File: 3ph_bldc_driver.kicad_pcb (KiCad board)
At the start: 4 copper layers, 20 parts, among them Q1 AON7264E-HXY, Q2 AON7264E-HXY, Q3 AON7264E-HXY, Q4 AON7264E-HXY, Q5 AON7264E-HXY, Q6 AON7264E-HXY

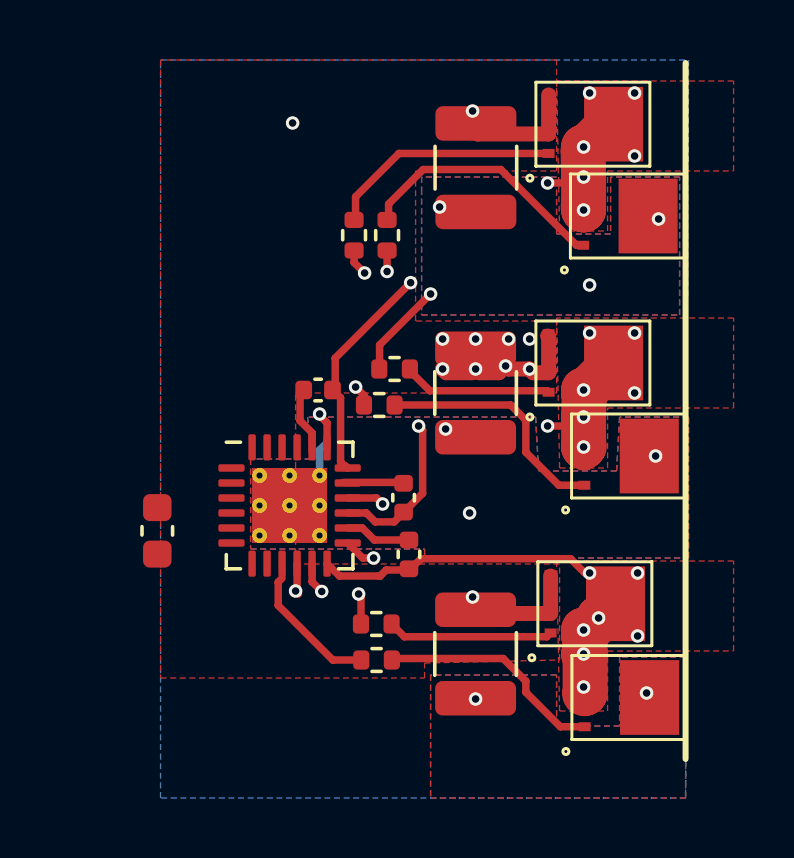
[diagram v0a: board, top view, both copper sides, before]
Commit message: found real parts for capacitors, added 0 ohm resistors, added diode footprints for src line
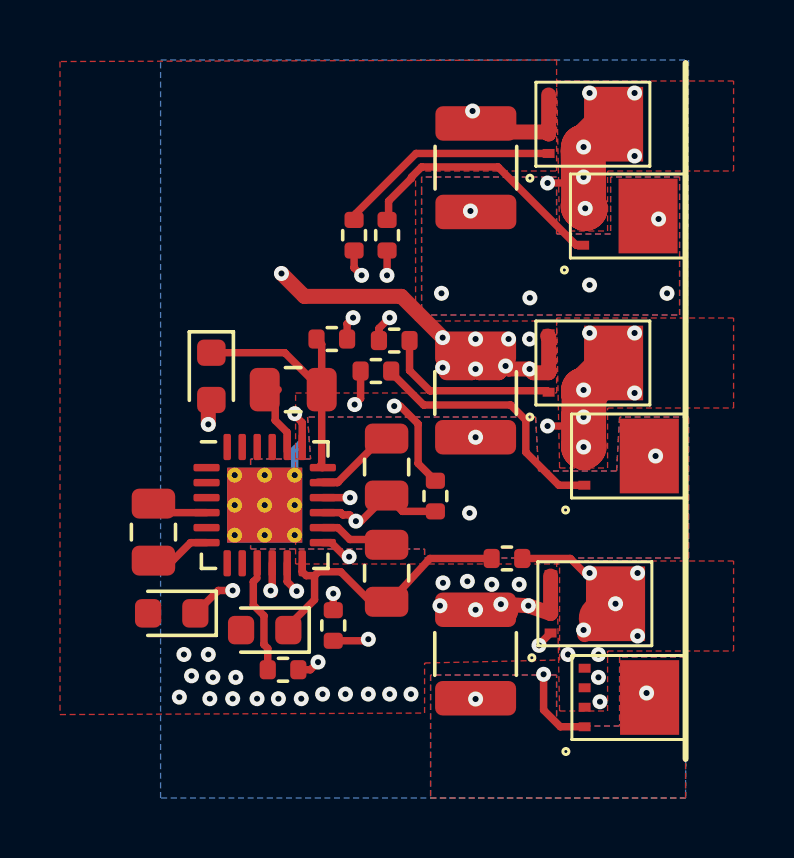
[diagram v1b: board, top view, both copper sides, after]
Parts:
- added D1: D, Diode_SMD:D_0603_1608Metric, F.Cu at (155.1, 96.5)
- added D2: D, Diode_SMD:D_0603_1608Metric, F.Cu at (153.8, 104.4)
- added D3: D, Diode_SMD:D_0603_1608Metric, F.Cu at (156.9, 105.0)
- added R7: 0R, Resistor_SMD:R_0402_1005Metric, F.Cu at (159.1, 95.3)
- added R8: 0R, Resistor_SMD:R_0402_1005Metric, F.Cu at (162.6, 100.5)
- added R9: 0R, Resistor_SMD:R_0402_1005Metric, F.Cu at (164.9, 102.6)
- C1, C2, C3: value C -> 1u; footprint Capacitor_SMD:C_0402_1005Metric -> Capacitor_SMD:C_0805_2012Metric
- C4: value C -> 10u; footprint Capacitor_SMD:C_0603_1608Metric -> Capacitor_SMD:C_0805_2012Metric
- C5, C6, C7: value C -> 10u
- moved R6 3.13 mm to (157.5, 106.3)
- moved R5 1.43 mm to (159.2, 104.8), turned to -90 degrees
- moved C2 1.17 mm to (160.9, 99.6)
- moved R4 1.14 mm to (160.6, 96.4)
- moved C3 0.98 mm to (160.9, 103.1)
- moved R3 0.95 mm to (161.2, 95.4)
- moved C1 0.83 mm to (157.8, 97.0)
- moved U1 0.83 mm to (156.9, 100.8)
- moved C4 0.13 mm to (153.2, 101.7)
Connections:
- C1 pad 2: /inverter/INV_OUT_A -> Net-(D1-K)
- C2 pad 2: /inverter/INV_OUT_B -> Net-(D2-K)
- C3 pad 2: /inverter/INV_OUT_C -> Net-(D3-K)
- U1 pad 12: /inverter/INV_OUT_C -> Net-(D3-K)
- U1 pad 15: /inverter/INV_OUT_B -> Net-(D2-K)
- U1 pad 18: /inverter/INV_OUT_A -> Net-(D1-K)
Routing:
- net Net-(D2-K): track 0.00 -> 13.9 mm, vias 0 -> 2
- net Net-(D3-K): track 0.00 -> 10.2 mm
- net GND: track 1.13 -> 11.1 mm, vias 8 -> 12
- net /inverter/INV_OUT_C: track 15.5 -> 5.96 mm, vias 7 -> 9
- net Net-(D1-K): track 0.00 -> 8.66 mm
- net +BATT: track 11.9 -> 19.0 mm, vias 11 -> 34
- net /inverter/INV_OUT_A: track 21.0 -> 15.4 mm
- net Net-(U1-GHB): track 12.2 -> 8.36 mm
- net Net-(Q6-G): track 7.60 -> 11.3 mm, vias 0 -> 2
- net Net-(Q5-G): track 5.53 -> 7.63 mm, vias 0 -> 2
- net +12V: track 0.00 -> 1.90 mm
- net Net-(U1-BSTB): track 2.03 -> 3.63 mm
- net /inverter/INV_OUT_B: track 14.5 -> 13.0 mm
- net Net-(U1-GLC): track 4.48 -> 3.31 mm
- net Net-(Q3-G): track 4.94 -> 5.93 mm
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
